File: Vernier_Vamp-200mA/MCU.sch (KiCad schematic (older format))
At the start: 9 parts

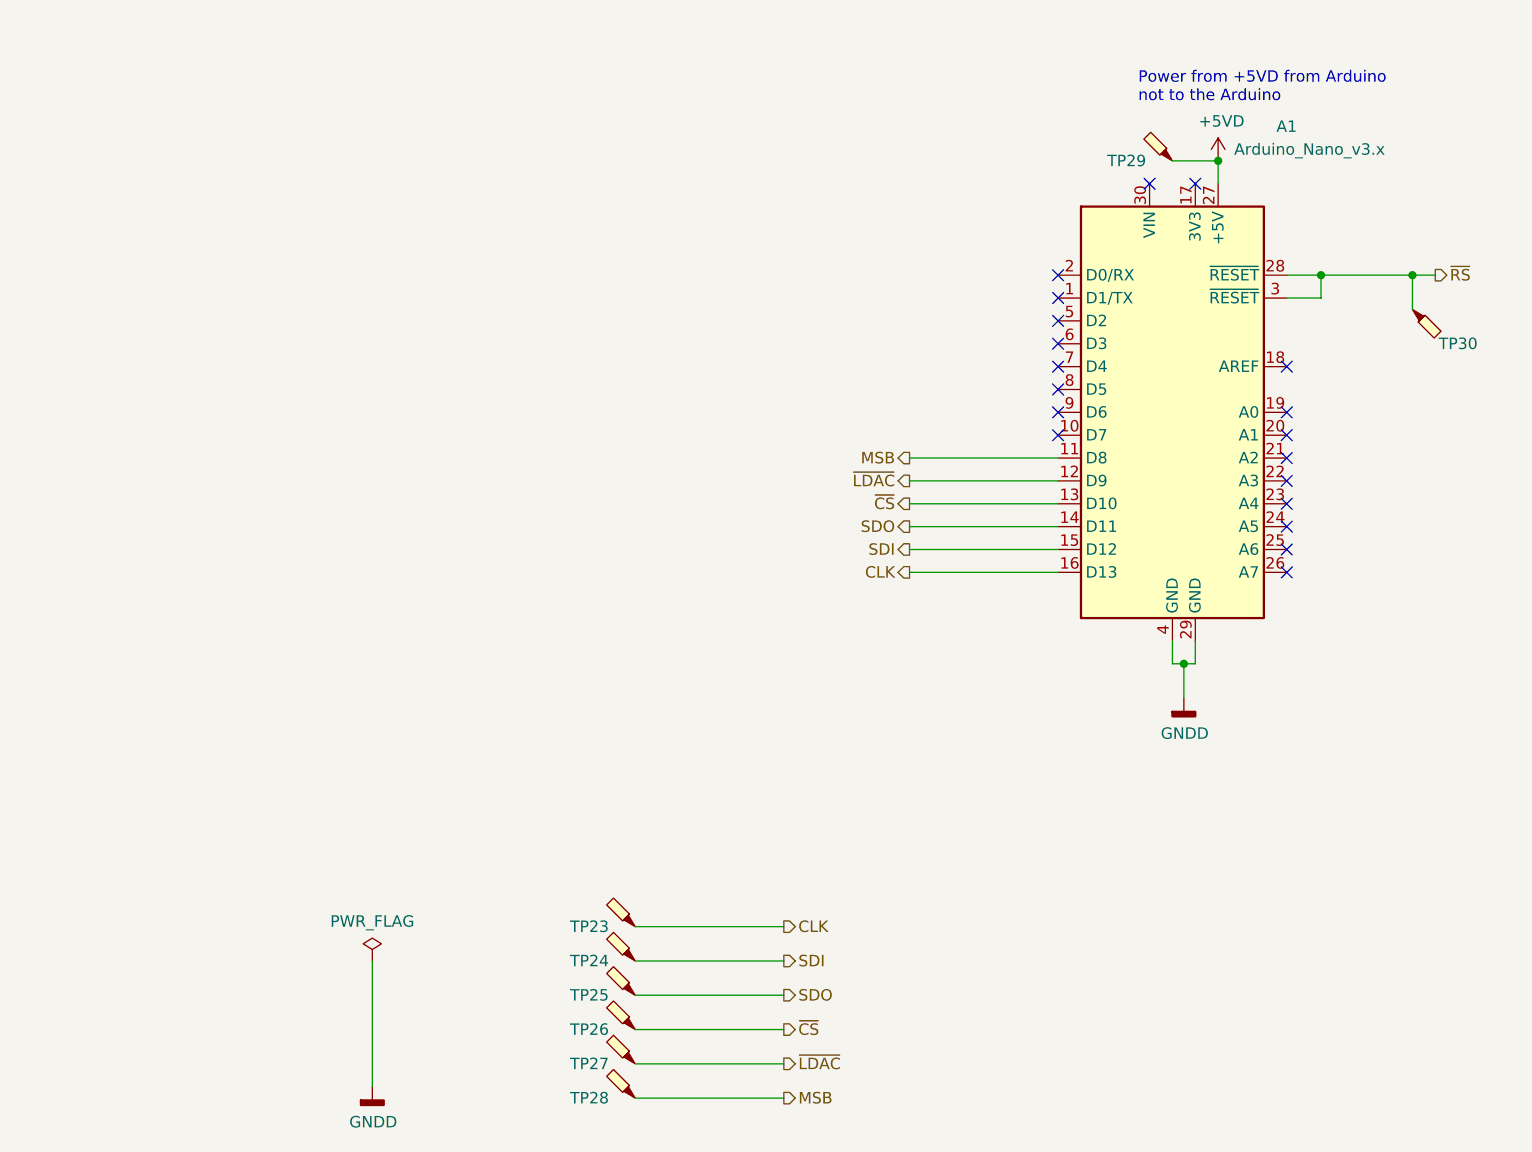
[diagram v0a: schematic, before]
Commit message: Coil driver version 1.0B
Updated coil driver 200mA version with fixes requested by Iain.
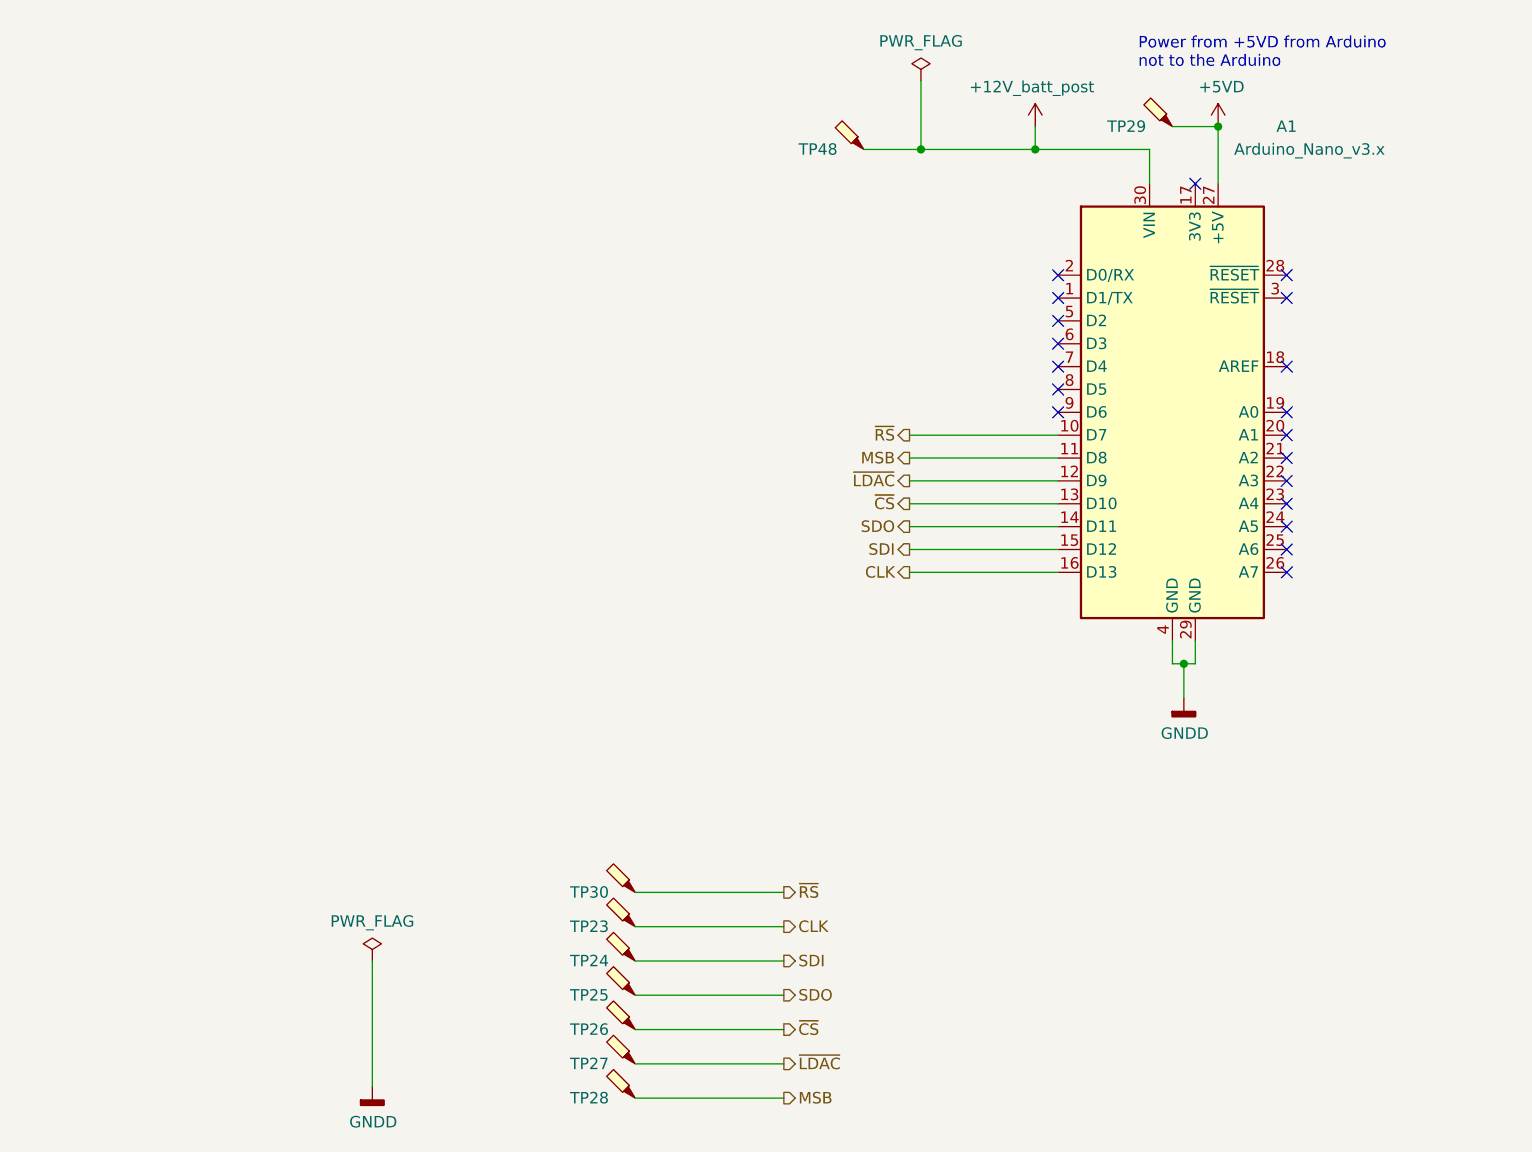
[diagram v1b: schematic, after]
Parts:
- added TP48: TestPoint_Probe, TestPoint:TestPoint_Pad_D1.0mm, symbol Connector:TestPoint_Probe
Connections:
- net ~RS: now also A1.10 (D7); no longer A1.28 (~RESET), A1.3 (~RESET)
- net +12V_batt_post: now reaches A1.30 (VIN)
- net +12V_batt_post: now also TP48.1
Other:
- moved on the sheet: TP29, TP30

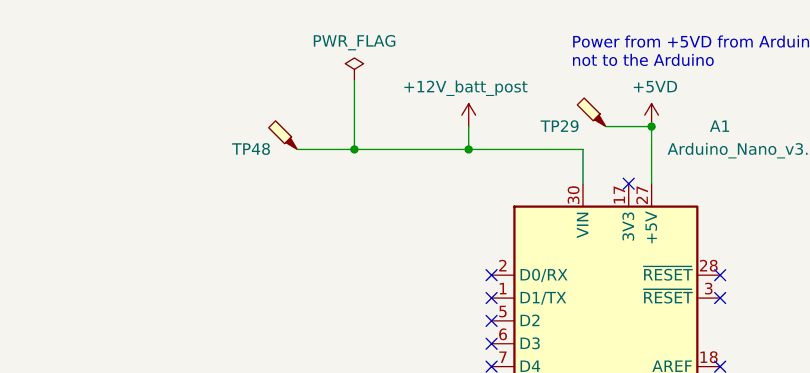
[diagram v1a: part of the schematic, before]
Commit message: Schematic and layout changes
Schematic updates:
- Added extra comments
- Added description (BNC channels)
- Moved mounting holes to the title block
- Added an option for connecting low battery indicatior LEDs to either +12V or GND (Comparator pulls to -12V)
- Added a 0R resistor for connecting +12V to Vin of nano
Layout:
- Added board ID and datecode on both sides
- Fixed priority of GND copper islands that were causing issues
- Changed the ground plane to be solid on the connection point (still not ideal but better)
- All components with thermal vias require tented vias so left as default
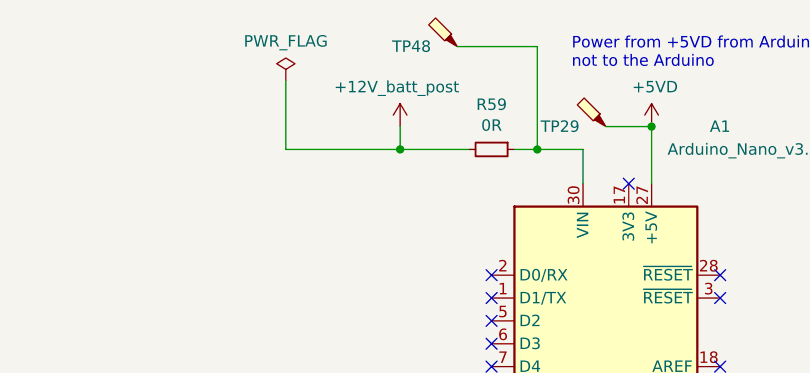
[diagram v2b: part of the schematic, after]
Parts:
- added R59: 0R, Resistor_SMD:R_0603_1608Metric_Pad1.05x0.95mm_HandSolder, symbol Device:R_Small
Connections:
- net +12V_batt_post: now also R59.2; no longer A1.30 (VIN), TP48.1
- new net: A1.30 (VIN), R59.1, TP48.1
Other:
- moved on the sheet: TP48
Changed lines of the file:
@@
 $Descr A4 11693 8268
 encoding utf-8
-Sheet 6 7
+Sheet 5 7
 Title "\"Vernier Vamp\" Coil Driver - 200mA"
 Date "2020-04-27"
@@
 NoConn ~ 6350 3300
 Wire Wire Line
-	5250 2550 5250 2650
-Wire Wire Line
-	5250 2650 5750 2650
+	4950 2550 4950 2650
+Wire Wire Line
+	4950 2650 5250 2650
 $Comp
 L custom_power_rails:+12V_batt_post #PWR?
 U 1 1 5ECA4E39
-P 5250 2550
+P 4950 2550
 AR Path="/5E1DD6A9/5EA9C7F8/5ECA4E39" Ref="#PWR?"  Part="1"
 AR Path="/5E1DEB8C/5ECA4E39" Ref="#PWR0210"  Part="1"
-F 0 "#PWR0210" H 5250 2500 50  0001 C CNN
-F 1 "+12V_batt_post" H 5235 2723 50  0000 C CNN
-F 2 "" H 5250 2550 50  0001 C CNN
-F 3 "" H 5250 2550 50  0001 C CNN
-	1    5250 2550
+F 0 "#PWR0210" H 4950 2500 50  0001 C CNN
+F 1 "+12V_batt_post" H 4935 2723 50  0000 C CNN
+F 2 "" H 4950 2550 50  0001 C CNN
+F 3 "" H 4950 2550 50  0001 C CNN
+	1    4950 2550
 	1    0    0    -1
 $EndComp
@@
 L power:PWR_FLAG #FLG?
 U 1 1 5EA5082E
-P 4750 2350
+P 4450 2350
 AR Path="/5E1DD6A9/5EA5082E" Ref="#FLG?"  Part="1"
 AR Path="/5E1DD6A9/5E9C5630/5EA5082E" Ref="#FLG?"  Part="1"
 AR Path="/5E1DD6A9/5EA9C7F8/5EA5082E" Ref="#FLG?"  Part="1"
 AR Path="/5E1DEB8C/5EA5082E" Ref="#FLG0105"  Part="1"
-F 0 "#FLG0105" H 4750 2425 50  0001 C CNN
-F 1 "PWR_FLAG" H 4750 2523 50  0000 C CNN
-F 2 "" H 4750 2350 50  0001 C CNN
-F 3 "~" H 4750 2350 50  0001 C CNN
-	1    4750 2350
-	1    0    0    -1
-$EndComp
-Wire Wire Line
-	5250 2650 4750 2650
-Wire Wire Line
-	4750 2650 4750 2350
-Connection ~ 5250 2650
+F 0 "#FLG0105" H 4450 2425 50  0001 C CNN
+F 1 "PWR_FLAG" H 4450 2523 50  0000 C CNN
+F 2 "" H 4450 2350 50  0001 C CNN
+F 3 "~" H 4450 2350 50  0001 C CNN
+	1    4450 2350
+	1    0    0    -1
+$EndComp
+Wire Wire Line
+	4950 2650 4450 2650
+Wire Wire Line
+	4450 2650 4450 2350
 $Comp
 L Connector:TestPoint_Probe TP48
 U 1 1 5EC0EB3C
-P 4500 2650
-F 0 "TP48" V 4500 2850 50  0000 C CNN
-F 1 "TestPoint_Probe" V 4699 2705 50  0001 C CNN
-F 2 "TestPoint:TestPoint_Pad_D1.0mm" H 4700 2650 50  0001 C CNN
-F 3 "~" H 4700 2650 50  0001 C CNN
-	1    4500 2650
-	0    -1   -1   0
-$EndComp
-Wire Wire Line
-	4500 2650 4750 2650
-Connection ~ 4750 2650
+P 5200 2200
+F 0 "TP48" V 5200 2400 50  0000 C CNN
+F 1 "TestPoint_Probe" V 5399 2255 50  0001 C CNN
+F 2 "TestPoint:TestPoint_Pad_D1.0mm" H 5400 2200 50  0001 C CNN
+F 3 "~" H 5400 2200 50  0001 C CNN
+	1    5200 2200
+	0    -1   -1   0
+$EndComp
+$Comp
+L Device:R_Small R59
+U 1 1 5EB1CFC9
+P 5350 2650
+F 0 "R59" V 5154 2650 50  0000 C CNN
+F 1 "0R" V 5245 2650 50  0000 C CNN
+F 2 "Resistor_SMD:R_0603_1608Metric_Pad1.05x0.95mm_HandSolder" H 5350 2650 50  0001 C CNN
+F 3 "~" H 5350 2650 50  0001 C CNN
+	1    5350 2650
+	0    1    1    0
+$EndComp
+Connection ~ 4950 2650
+Wire Wire Line
+	5750 2650 5550 2650
+Wire Wire Line
+	5550 2200 5550 2650
+Wire Wire Line
+	5200 2200 5550 2200
+Connection ~ 5550 2650
+Wire Wire Line
+	5550 2650 5450 2650
 $EndSCHEMATC

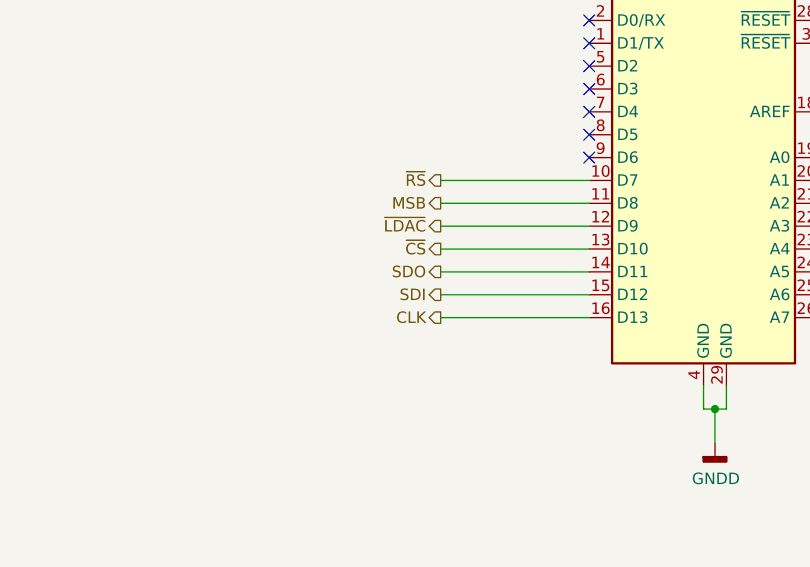
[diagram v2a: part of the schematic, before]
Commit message: 1.0C Initial commit
-Fixed amplifier output
-Changed connectors to IDC
-Via perimeter added
TODO:
Add shielding over analogue section
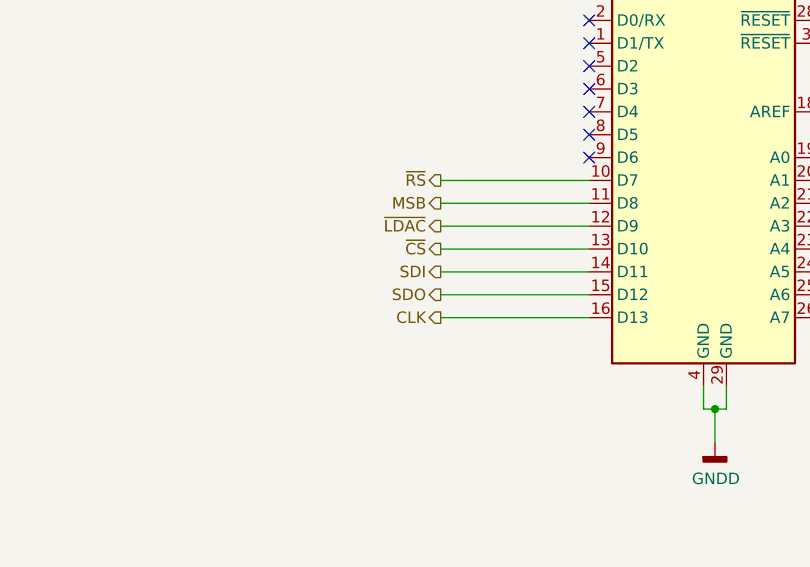
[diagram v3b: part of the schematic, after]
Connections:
- net SDI: now also A1.14 (D11); no longer A1.15 (D12)
- net SDO: now also A1.15 (D12); no longer A1.14 (D11)
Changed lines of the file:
@@
 Text HLabel 4700 4200 0    50   Output ~ 0
 ~CS
+Text HLabel 4700 4300 0    50   Output ~ 0
+SDI
 Text HLabel 4700 4400 0    50   Output ~ 0
-SDI
-Text HLabel 4700 4300 0    50   Output ~ 0
 SDO
 Wire Wire Line
@@
 	4700 4200 5350 4200
 Wire Wire Line
+	4700 4300 5350 4300
+Wire Wire Line
 	4700 4400 5350 4400
-Wire Wire Line
-	4700 4300 5350 4300
 NoConn ~ 5350 3700
 NoConn ~ 5350 3600
